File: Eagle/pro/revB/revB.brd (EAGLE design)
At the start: 65 x 100 mm, 13 parts, among them IC1 ATMEGA644A, Q1 20MHz

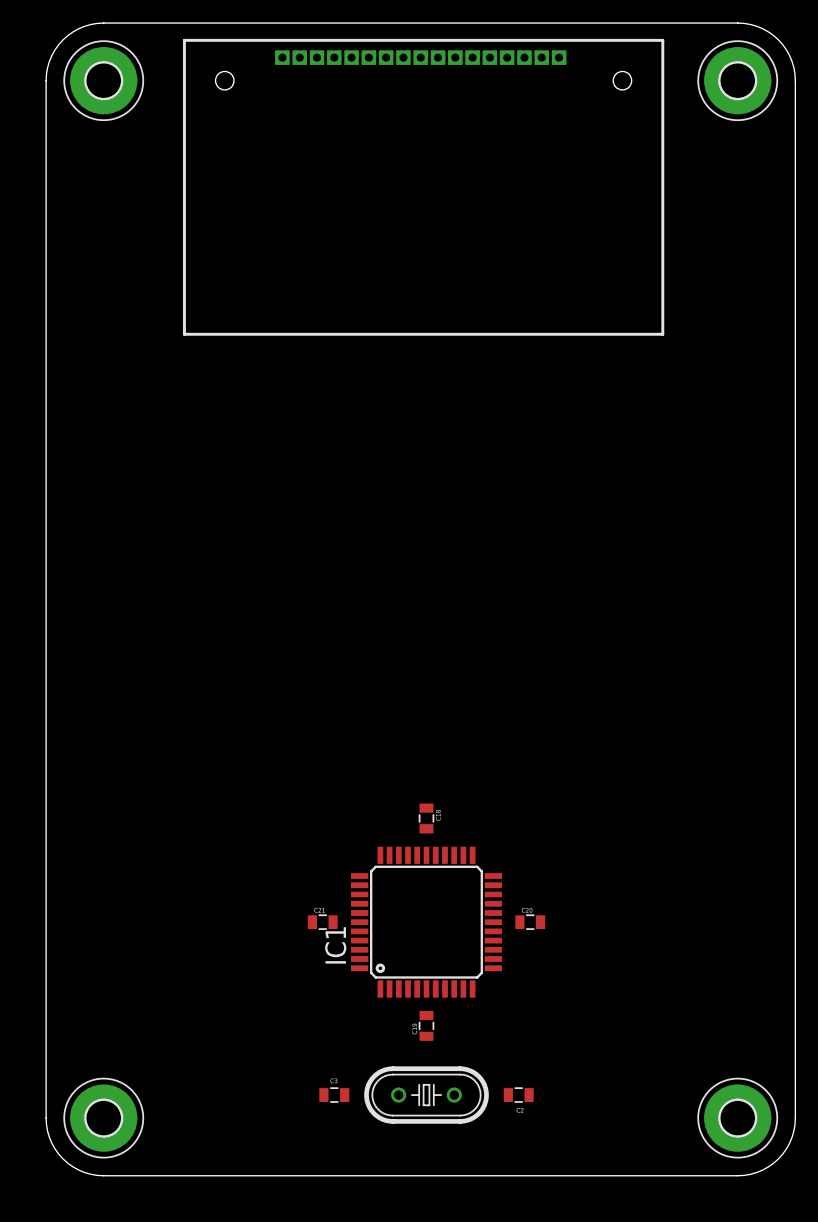
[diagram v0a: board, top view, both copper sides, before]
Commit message: new pcb with a 644
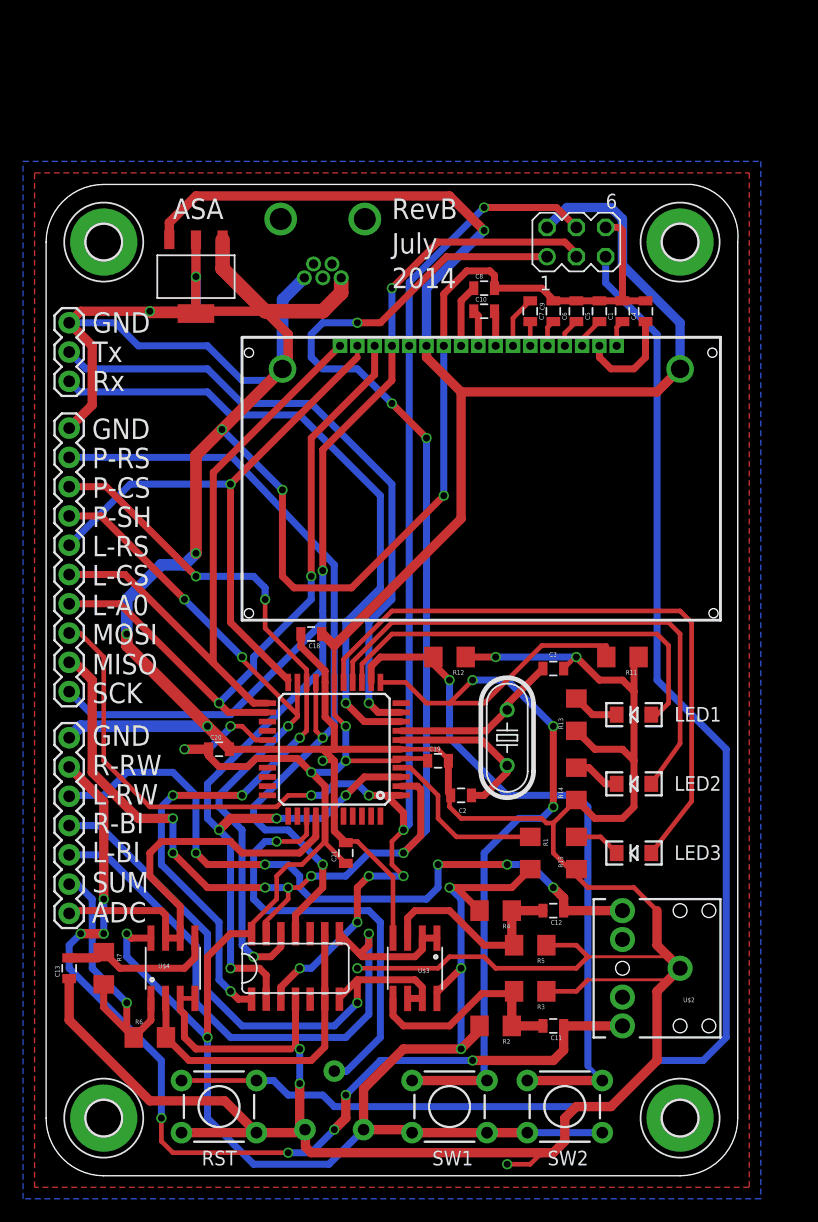
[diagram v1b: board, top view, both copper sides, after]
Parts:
- added C1, C10, C11, C12, C4, C5, C6, C7, C8, C9: 100nF, SparkFun:0805
- added C13: 22pF, SparkFun:0805
- added JP1: (no value), SparkFun-Connectors:1X03
- added JP2: M10", SparkFun-Connectors:1X10
- added JP3: (no value), SparkFun-Connectors:1X07
- added LED1, LED2, LED3: (no value), SparkFun:LED-1206
- added R1, R11, R12: 4.7K, SparkFun:1206
- added R13, R14, R15: 68, SparkFun:1206
- added R2, R3, R6: 100K, SparkFun:1206
- added R4, R5: 100k, SparkFun:1206
- added R7: 330K, SparkFun:1206
- added S1, S2, S3: (no value), SparkFun:TACTILE-PTH
- added SV1: (no value), con-lstb:MA03-2
- added U$2: AUDIO-JACKPTH, SparkFun:AUDIO-JACK
- added U$3, U$4: LM393, SparkFun:SO08
- added U$5: POTTRIM, SparkFun:TRIM_POT
- added U1: MCP42XXX, SparkFun:SO014
- added U2: MCP1826S-3302E/DB, MCP1826S:SOT230P700X180-4N
- added X2: USB-MB-H, SparkFun:USB-MB-H
- moved C3 41.6 mm to (44.0, 44.0)
- moved Q1 31.8 mm to (40.0, 38.0), turned to 90 degrees
- moved C20 30.9 mm to (15.0, 37.0)
- moved C2 26.5 mm to (36.0, 33.0)
- moved U$1 25.5 mm to (17.0, 48.0)
- moved C19 23.0 mm to (34.0, 36.0), turned to 0 degrees
- moved C18 18.9 mm to (23.0, 47.0), turned to 180 degrees
- moved IC1 17.0 mm to (25.0, 37.0), turned to 180 degrees
- moved H4 14.9 mm to (55.0, 81.0)
- moved H3 14.0 mm to (5.00, 81.0)
- moved C21 6.32 mm to (26.0, 28.0), turned to 90 degrees
- moved H2 5.00 mm to (55.0, 5.00)
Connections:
- new net BIAS_LEFT: JP3.5, U$3.1, U$3.2, U1.8
- new net BIAS_RIGHT: JP3.4, U$3.6, U$3.7, U1.7
- new net D+: IC1.42
- new net D-: IC1.43
- new net DEBUG_RX: IC1.9, JP1.3
- new net DEBUG_TX: IC1.10, JP1.2
- new net LCD_A0: IC1.24, JP2.4, U$1.15
- new net LCD_CS: IC1.23, JP2.5, U$1.17
- new net LCD_RST: IC1.22, JP2.6, U$1.16
- new net LED1: IC1.14, LED1.A
- new net LED2: IC1.15, LED2.A
- new net LED3: IC1.16, LED3.A
- new net MISO: IC1.2, JP2.2, SV1.1, U1.13
- new net MOSI: IC1.1, JP2.3, SV1.4, U$1.13, U1.3
- new net N$10: C6.1, U$1.4
- new net N$11: C7.1, U$1.5
- new net N$12: C8.1, U$1.10
- new net N$13: S1.3, S1.4, SV1.5
- new net N$15: C11.2, R2.1, R3.2, U$3.5
- new net N$16: C12.2, R4.1, R5.2, U$3.3
- new net N$17: C13.2, R7.1, U$4.5
- new net N$20: U2.1, X2.VBUS
- new net N$22: LED1.C, R13.2
- new net N$23: LED2.C, R14.2
- new net N$24: LED3.C, R15.2
- new net N$3: C9.2, U$1.6
- new net N$4: C9.1, U$1.7
- new net N$5: C10.2, U$1.8
- new net N$6: C10.1, U$1.9
- new net N$7: C1.1, U$1.1
- new net N$8: C4.1, U$1.2
- new net N$9: C5.1, U$1.3
- new net POT_CS: IC1.20, JP2.8, U1.1
- new net POT_RST: IC1.19, JP2.9, U1.11
- new net POT_SHDW: IC1.21, JP2.7, U1.12
- new net RAW_LEFT: C12.1, JP3.3, U$2.5
- new net RAW_RIGHT: C11.1, JP3.2, U$2.2
- new net RESET: IC1.4, R1.1
- new net SCK: IC1.3, JP2.1, SV1.3, U$1.14, U1.2
- new net SUM: R6.2, U$4.2, U1.6, U1.9
- new net SUMMED: JP3.6, R6.1, R7.2, U$4.1
- new net SW1: IC1.12, R11.2, S2.1, S2.2
- new net SW2: IC1.13, R12.2, S3.1, S3.2
- new net TO_ADC: IC1.37, JP3.7, U$4.6, U$4.7
- new net USER_TRIM: IC1.36, U$5.1
- net GND: now also C1.2, C13.1, C4.2, C5.2, C6.2, C7.2, C8.2, JP1.1, JP2.10, JP3.1, R11.1, R12.1, R13.1, R14.1, R15.1, R3.1, R5.1, S1.1, S1.2, SV1.6, U$1.11, U$1.K, U$2.1, U$3.4, U$4.3, U$4.4, U$5.2, U1.4, U2.2, U2.4, X2.GND
- net VCC: now also R1.2, R2.2, R4.2, S2.3, S2.4, S3.3, S3.4, SV1.2, U$1.12, U$1.A, U$3.8, U$4.8, U$5.3, U1.14, U2.3
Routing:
- net GND: track 0.00 -> 501.9 mm, vias 0 -> 15
- net VCC: track 0.00 -> 297.2 mm, vias 0 -> 11
- net SCK: track 0.00 -> 134.1 mm, vias 0 -> 6
- net MOSI: track 0.00 -> 133.3 mm, vias 0 -> 8
- net MISO: track 0.00 -> 132.6 mm, vias 0 -> 9
- net N$13: track 0.00 -> 122.7 mm
- net RAW_RIGHT: track 0.00 -> 86.8 mm, vias 0 -> 8
- net SW1: track 0.00 -> 76.4 mm, vias 0 -> 3
- net POT_RST: track 0.00 -> 71.6 mm, vias 0 -> 2
- net POT_CS: track 0.00 -> 70.5 mm, vias 0 -> 6
- net RAW_LEFT: track 0.00 -> 61.6 mm, vias 0 -> 5
- net SW2: track 0.00 -> 60.0 mm, vias 0 -> 1
- net POT_SHDW: track 0.00 -> 58.8 mm, vias 0 -> 4
- net LCD_A0: track 0.00 -> 57.7 mm, vias 0 -> 2
- net BIAS_LEFT: track 0.00 -> 56.7 mm, vias 0 -> 1
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- added copper zone on layer 16, net GND
- added copper zone on layer 1, net VCC
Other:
- board size 65 x 100 mm -> 60 x 86 mm
- board text added: "2014"
- board text added: "ADC"
- board text added: "ASA"
- board text added: "GND"
- board text added: "July"
- board text added: "L-A0"
- board text added: "L-BI"
- board text added: "L-CS"
- board text added: "L-RS"
- board text added: "L-RW"
- board text added: "LED1"
- board text added: "LED2"
- board text added: "LED3"
- board text added: "MISO"
- board text added: "MOSI"
- board text added: "P-CS"
- board text added: "P-RS"
- board text added: "P-SH"
- board text added: "R-BI"
- board text added: "R-RW"
- board text added: "RST"
- board text added: "RevB"
- board text added: "Rx"
- board text added: "SCK"
- board text added: "SUM"
- board text added: "SW1"
- board text added: "SW2"
- board text added: "Tx"
